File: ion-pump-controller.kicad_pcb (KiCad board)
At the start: 2 copper layers, 47 parts, among them J1 Barrel_Jack, Q1 IRFP4668PbF, T1 Transformer_1P_1S, U1 TSR_1-2433, U2 MCP6001R, U3 TC4422, U4 TSR1.5-24120E

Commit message: 1.0 version
these are the new schematic and pcb files for what should be the theoretically working board
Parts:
- removed U3: TC4422, Package_DIP:DIP-8_W7.62mm
- added C9: 2.5nf, Capacitor_THT:C_Disc_D14.5mm_W5.0mm_P10.00mm, F.Cu at (171.0, 58.0)
- added D9: UF5408, Diode_THT:D_DO-201AD_P15.24mm_Horizontal, F.Cu at (188.0, 83.4)
- added J2: START BUTTON, TerminalBlock_Phoenix:TerminalBlock_Phoenix_MKDS-1,5-2_1x02_P5.00mm_Horizontal, F.Cu at (95.7, 187.0)
- added J3: SCREEN, Connector_Phoenix_SPT:PhoenixContact_SPT_2.5_4-H-5.0_1x04_P5.0mm_Horizontal, F.Cu at (96.8, 152.0)
- added J4: DRAIN BUTTON, TerminalBlock_Phoenix:TerminalBlock_Phoenix_MKDS-1,5-2_1x02_P5.00mm_Horizontal, F.Cu at (41.0, 187.0)
- added J5: LIGHT, TerminalBlock_Phoenix:TerminalBlock_Phoenix_MKDS-1,5-2_1x02_P5.00mm_Horizontal, F.Cu at (68.2, 187.2)
- added J6: POWER SWITCH, TerminalBlock_Phoenix:TerminalBlock_Phoenix_MKDS-1,5-2_1x02_P5.00mm_Horizontal, F.Cu at (55.0, 30.0)
- added R22: 330, Resistor_THT:R_Axial_DIN0411_L9.9mm_D3.6mm_P25.40mm_Horizontal, F.Cu at (84.0, 108.3)
- added R23: 330, Resistor_THT:R_Axial_DIN0411_L9.9mm_D3.6mm_P25.40mm_Horizontal, F.Cu at (43.6, 137.0)
- added R24: 1k, Resistor_THT:R_Axial_DIN0411_L9.9mm_D3.6mm_P25.40mm_Horizontal, F.Cu at (103.7, 69.0)
- added R25: 47k, Resistor_THT:R_Axial_DIN0411_L9.9mm_D3.6mm_P25.40mm_Horizontal, F.Cu at (181.0, 53.3)
- added U5: 6N137, Package_DIP:DIP-8_W7.62mm, F.Cu at (73.2, 154.2)
- added U6: TC4421, Package_DIP:DIP-8_W7.62mm, F.Cu at (96.0, 47.9)
- moved RV1 45.7 mm to (23.0, 153.0)
- moved U2 37.6 mm to (80.0, 81.0), turned to -90 degrees
- moved A1 34.1 mm to (46.0, 86.0)
- moved Q1 32.4 mm to (177.2, 97.5), turned to -90 degrees
- moved U4 29.6 mm to (103.5, 30.1), turned to 90 degrees
- moved RV2 25.3 mm to (23.0, 133.0)
- moved C1 18.6 mm to (272.0, 51.0)
- moved R1 11.9 mm to (232.9, 129.7)
- moved R2 11.9 mm to (232.9, 115.7)
- moved R3 11.9 mm to (232.9, 101.7)
- moved R4 11.9 mm to (232.9, 87.7)
- moved R5 11.9 mm to (232.9, 73.7)
- moved R6 10.1 mm to (222.8, 139.9)
- moved R10 10.1 mm to (222.8, 84.0)
- moved R7 10.1 mm to (222.8, 126.0)
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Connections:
- A1 pad 17: unconnected-(A1-SDA/IO23-Pad17) -> Net-(A1-SDA/IO23)
- A1 pad 18: unconnected-(A1-SCL/IO22-Pad18) -> Net-(A1-SCL/IO22)
- A1 pad 19: unconnected-(A1-A6/IO14-Pad19) -> Net-(A1-A6/IO14)
- A1 pad 20: unconnected-(A1-A7/IO32-Pad20) -> Net-(A1-A7/IO32)
- A1 pad 23: unconnected-(A1-A10/IO27-Pad23) -> Net-(A1-A10/IO27)
- A1 pad 5: /PWM output -> Net-(A1-DAC2/A0)
- J1 pad 1: +24V -> Net-(J6-Pin_2)
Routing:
- net +3V3: track 0.00 -> 250.7 mm, vias 0 -> 2
- net +24V: track 0.00 -> 194.8 mm
- net Net-(U2-+): track 0.00 -> 149.1 mm
- net Net-(U5-VO): track 0.00 -> 123.1 mm
- net GND: track 0.00 -> 116.9 mm, vias 0 -> 2
- net Net-(Q1-G): track 0.00 -> 94.6 mm
- net Net-(D9-A): track 0.00 -> 89.5 mm
- net Net-(A1-A7/IO32): track 0.00 -> 81.0 mm, vias 0 -> 2
- net Net-(A1-A6/IO14): track 0.00 -> 80.1 mm
- net Net-(J5-Pin_1): track 0.00 -> 73.4 mm, vias 0 -> 2
- net /1kV: track 0.00 -> 68.8 mm
- net /final Vout: track 0.00 -> 57.8 mm
- net /ramp time controller: track 0.00 -> 57.7 mm
- net /feedback input: track 0.00 -> 56.5 mm, vias 0 -> 2
- net Net-(A1-SDA/IO23): track 0.00 -> 48.2 mm, vias 0 -> 2
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- added copper zone on B.Cu, net GND
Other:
- board outline added: 273.1 x 186.1 mm

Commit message: v1.1
split the ground plane to high and low voltage, made the output two pads instead of screw terminals
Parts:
- added J7: output -, TestPoint:TestPoint_Pad_4.0x4.0mm, F.Cu at (253.1, 147.6)
- added J8: output +, TestPoint:TestPoint_Pad_4.0x4.0mm, F.Cu at (273.0, 137.0)
- added NT1: NetTie_2, NetTie:NetTie-2_SMD_Pad2.0mm, B.Cu at (144.9, 96.8)
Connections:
- C2 pad 2: GND -> Earth
- C8 pad 1: /final Vout -> Net-(D7-K)
- D1 pad 2: GND -> Earth
- D7 pad 1: /final Vout -> Net-(D7-K)
- D8 pad 2: /final Vout -> Net-(D7-K)
- Q1 pad 3: GND -> Earth
- R21 pad 2: GND -> Earth
- T1 pad 3: GND -> Earth
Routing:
- net GND: track 116.9 -> 47.2 mm
- net Earth: track 0.00 -> 69.8 mm
- net Net-(D7-K): track 0.00 -> 36.9 mm
- net /final Vout: track 57.8 -> 25.0 mm
- added copper zone on B.Cu, net Earth
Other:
- board text added: "3.3V pwr"
- board text added: "DRAIN BUTTON"
- board text added: "LIGHT BUTTON"
- board text added: "SCL"
- board text added: "SDA"
- board text added: "START BUTTON"
- board text added: "gnd"
- board text added: "high to low voltage gnd bridge"
- board text added: "this side will kill you!"
- board text added: "this side will not kill you!"

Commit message: v1.1
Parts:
- moved J8 1.00 mm to (273.0, 138.0)
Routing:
- net +24V: track 194.8 -> 235.8 mm
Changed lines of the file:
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@@
 	)
 	(setup
+		(stackup
+			(layer "F.SilkS"
+				(type "Top Silk Screen")
+			)
+			(layer "F.Paste"
+				(type "Top Solder Paste")
+			)
+			(layer "F.Mask"
+				(type "Top Solder Mask")
+				(thickness 0.01)
+			)
+			(layer "F.Cu"
+				(type "copper")
+				(thickness 0.035)
+			)
+			(layer "dielectric 1"
+				(type "core")
+				(thickness 1.51)
+				(material "FR4")
+				(epsilon_r 4.5)
+				(loss_tangent 0.02)
+			)
+			(layer "B.Cu"
+				(type "copper")
+				(thickness 0.035)
+			)
+			(layer "B.Mask"
+				(type "Bottom Solder Mask")
+				(thickness 0.01)
+			)
+			(layer "B.Paste"
+				(type "Bottom Solder Paste")
+			)
+			(layer "B.SilkS"
+				(type "Bottom Silk Screen")
+			)
+			(copper_finish "None")
+			(dielectric_constraints no)
+		)
 		(pad_to_mask_clearance 0)
 		(allow_soldermask_bridges_in_footprints no)
@@
 		(tags "test point SMD pad rectangle square")
 		(property "Reference" "J7"
-			(at 0 -2.898 0)
+			(at 3.9 0.4475 0)
 			(layer "F.SilkS")
 			(effects
@@
 	(footprint "TestPoint:TestPoint_Pad_4.0x4.0mm"
 		(layer "F.Cu")
-		(at 273 137)
+		(at 273 138)
 		(descr "SMD rectangular pad as test Point, square 4.0mm side length")
 		(tags "test point SMD pad rectangle square")
 		(property "Reference" "J8"
-			(at 0 -2.898 0)
+			(at 5 0 0)
 			(layer "F.SilkS")
 			(effects
@@
 	)
 	(segment
-		(start 116 16)
-		(end 103.46 28.54)
+		(start 161 80)
+		(end 151 90)
+		(width 1.5)
+		(layer "F.Cu")
+		(net 38)
+	)
+	(segment
+		(start 171 58)
+		(end 161 68)
+		(width 1.5)
+		(layer "F.Cu")
+		(net 38)
+	)
+	(segment
+		(start 105.150447 28.0615)
+		(end 103.46 29.751947)
+		(width 1.5)
+		(layer "F.Cu")
+		(net 38)
+	)
+	(segment
+		(start 133 78)
+		(end 133 47)
 		(width 1.5)
 		(layer "F.Cu")
@@
 	)
 	(segment
+		(start 114.0615 28.0615)
+		(end 105.150447 28.0615)
+		(width 1.5)
+		(layer "F.Cu")
+		(net 38)
+	)
+	(segment
+		(start 103.46 29.751947)
+		(end 103.46 30.1125)
+		(width 1.5)
+		(layer "F.Cu")
+		(net 38)
+	)
+	(segment
 		(start 55 30)
 		(end 64 30)
@@
 	)
 	(segment
-		(start 103.46 28.54)
-		(end 103.46 30.1125)
+		(start 161 68)
+		(end 161 80)
 		(width 1.5)
 		(layer "F.Cu")
@@
 	)
 	(segment
-		(start 171 58)
-		(end 129 16)
+		(start 133 47)
+		(end 114.0615 28.0615)
 		(width 1.5)
 		(layer "F.Cu")
@@
 	)
 	(segment
-		(start 194.3 53.3)
-		(end 195.25 54.25)
+		(start 145 90)
+		(end 133 78)
 		(width 1.5)
 		(layer "F.Cu")
@@
 	)
 	(segment
-		(start 129 16)
-		(end 116 16)
+		(start 194.3 53.3)
+		(end 195.25 54.25)
 		(width 1.5)
 		(layer "F.Cu")
@@
 		(layer "F.Cu")
 		(net 38)
+	)
+	(segment
+		(start 151 90)
+		(end 145 90)
+		(width 1.5)
+		(layer "F.Cu")
+		(net 38)

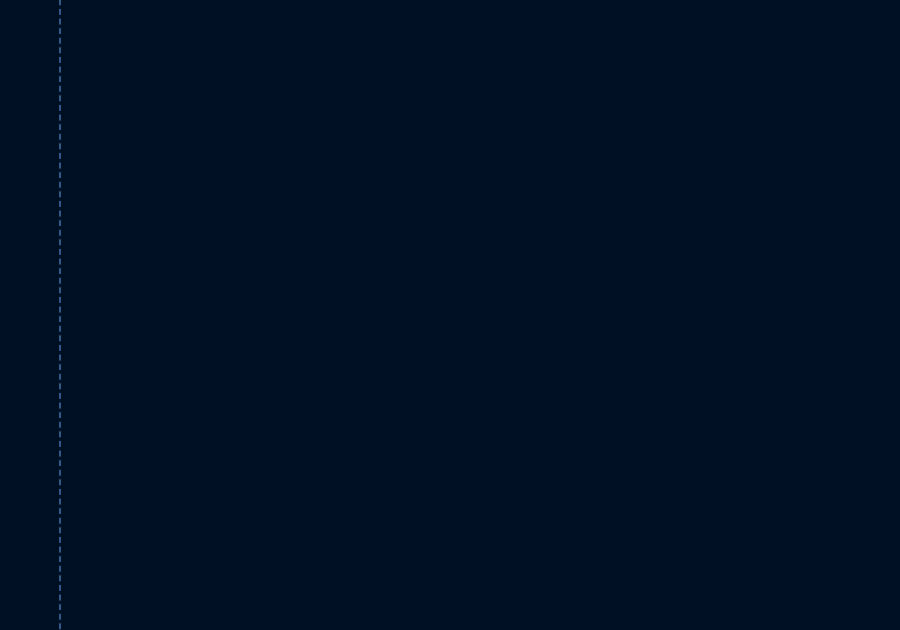
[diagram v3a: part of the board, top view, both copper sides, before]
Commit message: v1.1
added a pad for earth gnd
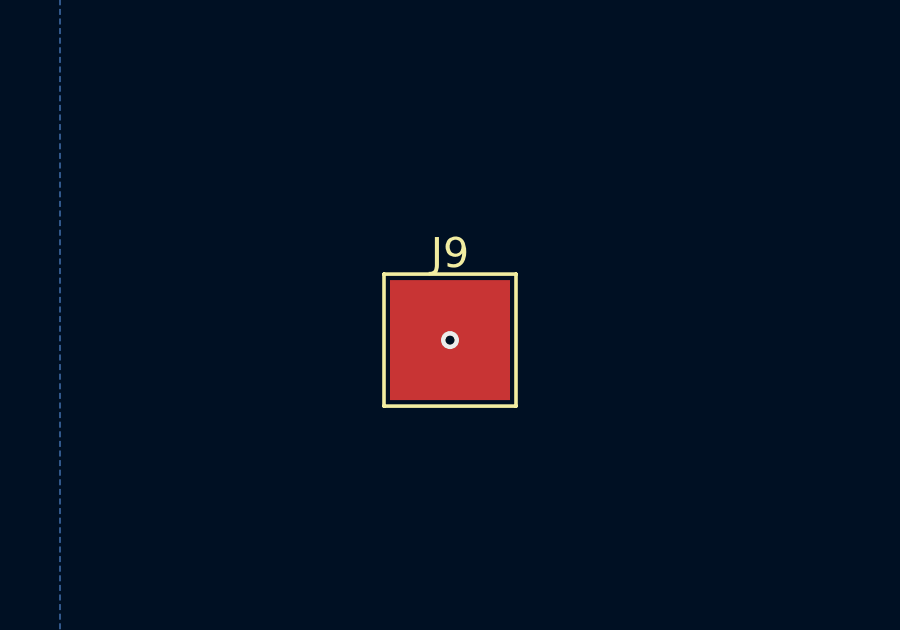
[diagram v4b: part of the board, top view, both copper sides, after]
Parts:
- added J9: earth terminal, TestPoint:TestPoint_Pad_4.0x4.0mm, F.Cu at (163.0, 176.0)
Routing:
- net Earth: vias 0 -> 1
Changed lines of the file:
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@@
 		)
 	)
+	(footprint "TestPoint:TestPoint_Pad_4.0x4.0mm"
+		(layer "F.Cu")
+		(at 163 176)
+		(descr "SMD rectangular pad as test Point, square 4.0mm side length")
+		(tags "test point SMD pad rectangle square")
+		(property "Reference" "J9"
+			(at 0 -2.898 0)
+			(layer "F.SilkS")
+			(effects
+				(font
+					(size 1 1)
+					(thickness 0.15)
+				)
+			)
+		)
+		(property "Value" "earth terminal"
+			(at 0 3.1 0)
+			(layer "F.Fab")
+			(effects
+				(font
+					(size 1 1)
+					(thickness 0.15)
+				)
+			)
+		)
+		(property "Datasheet" "~"
+			(at 0 0 0)
+			(unlocked yes)
+			(layer "F.Fab")
+			(hide yes)
+			(effects
+				(font
+					(size 1.27 1.27)
+					(thickness 0.15)
+				)
+			)
+		)
+		(property "Description" "Generic connector, single row, 01x01, script generated"
+			(at 0 0 0)
+			(unlocked yes)
+			(layer "F.Fab")
+			(hide yes)
+			(effects
+				(font
+					(size 1.27 1.27)
+					(thickness 0.15)
+				)
+			)
+		)
+		(property ki_fp_filters "Connector*:*_1x??_*")
+		(sheetname "/")
+		(sheetfile "ion-pump-controller.kicad_sch")
+		(attr exclude_from_pos_files)
+		(fp_line
+			(start -2.2 -2.2)
+			(end 2.2 -2.2)
+			(stroke
+				(width 0.12)
+				(type solid)
+			)
+			(layer "F.SilkS")
+		)
+		(fp_line
+			(start -2.2 2.2)
+			(end -2.2 -2.2)
+			(stroke
+				(width 0.12)
+				(type solid)
+			)
+			(layer "F.SilkS")
+		)
+		(fp_line
+			(start 2.2 -2.2)
+			(end 2.2 2.2)
+			(stroke
+				(width 0.12)
+				(type solid)
+			)
+			(layer "F.SilkS")
+		)
+		(fp_line
+			(start 2.2 2.2)
+			(end -2.2 2.2)
+			(stroke
+				(width 0.12)
+				(type solid)
+			)
+			(layer "F.SilkS")
+		)
+		(fp_line
+			(start -2.5 -2.5)
+			(end -2.5 2.5)
+			(stroke
+				(width 0.05)
+				(type solid)
+			)
+			(layer "F.CrtYd")
+		)
+		(fp_line
+			(start -2.5 -2.5)
+			(end 2.5 -2.5)
+			(stroke
+				(width 0.05)
+				(type solid)
+			)
+			(layer "F.CrtYd")
+		)
+		(fp_line
+			(start 2.5 2.5)
+			(end -2.5 2.5)
+			(stroke
+				(width 0.05)
+				(type solid)
+			)
+			(layer "F.CrtYd")
+		)
+		(fp_line
+			(start 2.5 2.5)
+			(end 2.5 -2.5)
+			(stroke
+				(width 0.05)
+				(type solid)
+			)
+			(layer "F.CrtYd")
+		)
+		(fp_text user "${REFERENCE}"
+			(at 0 -2.9 0)
+			(layer "F.Fab")
+			(effects
+				(font
+					(size 1 1)
+					(thickness 0.15)
+				)
+			)
+		)
+		(pad "1" smd rect
+			(at 0 0)
+			(size 4 4)
+			(layers "F.Cu" "F.Mask")
+			(net 70 "Earth")
+			(pinfunction "Pin_1")
+			(pintype "passive")
+		)
+		(embedded_fonts no)
+	)
 	(footprint "Resistor_THT:R_Axial_DIN0207_L6.3mm_D2.5mm_P10.16mm_Horizontal"
 		(layer "F.Cu")
@@
 		(net 70)
 	)
+	(via
+		(at 163 176)
+		(size 0.6)
+		(drill 0.3)
+		(layers "F.Cu" "B.Cu")
+		(free yes)
+		(net 70)
+	)
